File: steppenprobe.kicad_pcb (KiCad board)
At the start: 2 copper layers, 50 x 60 mm, 83 parts, among them J1 USB_C_Receptacle_USB2.0, J2 Conn_ST_STDC14, J4 Conn_01x16, Q1 2N7002, SW1 SW_SPDT, SW2 SW_Push, U1 FT2232H, U10 74LVC1G125, U11 74LVC1G125, U12 74LVC1G125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

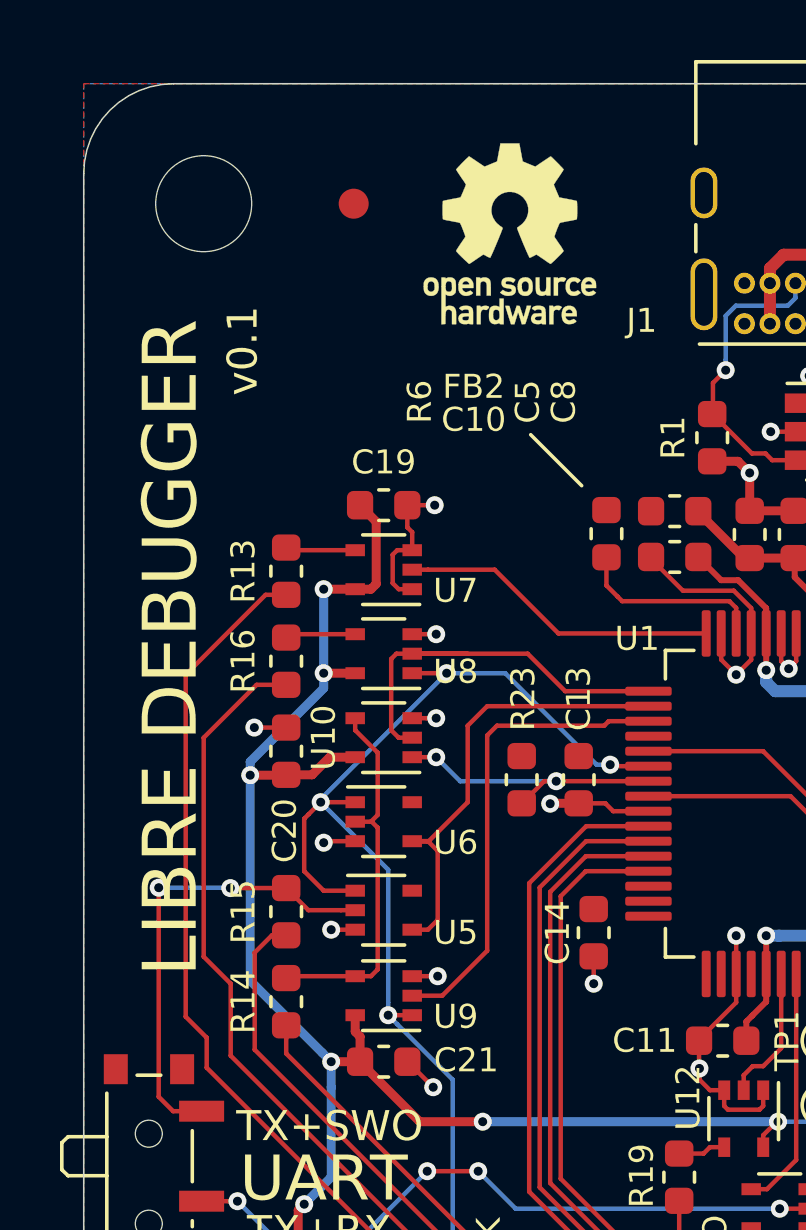
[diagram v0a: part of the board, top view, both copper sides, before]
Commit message: Add QR and new project URL. Finish bottom side silkscreen.
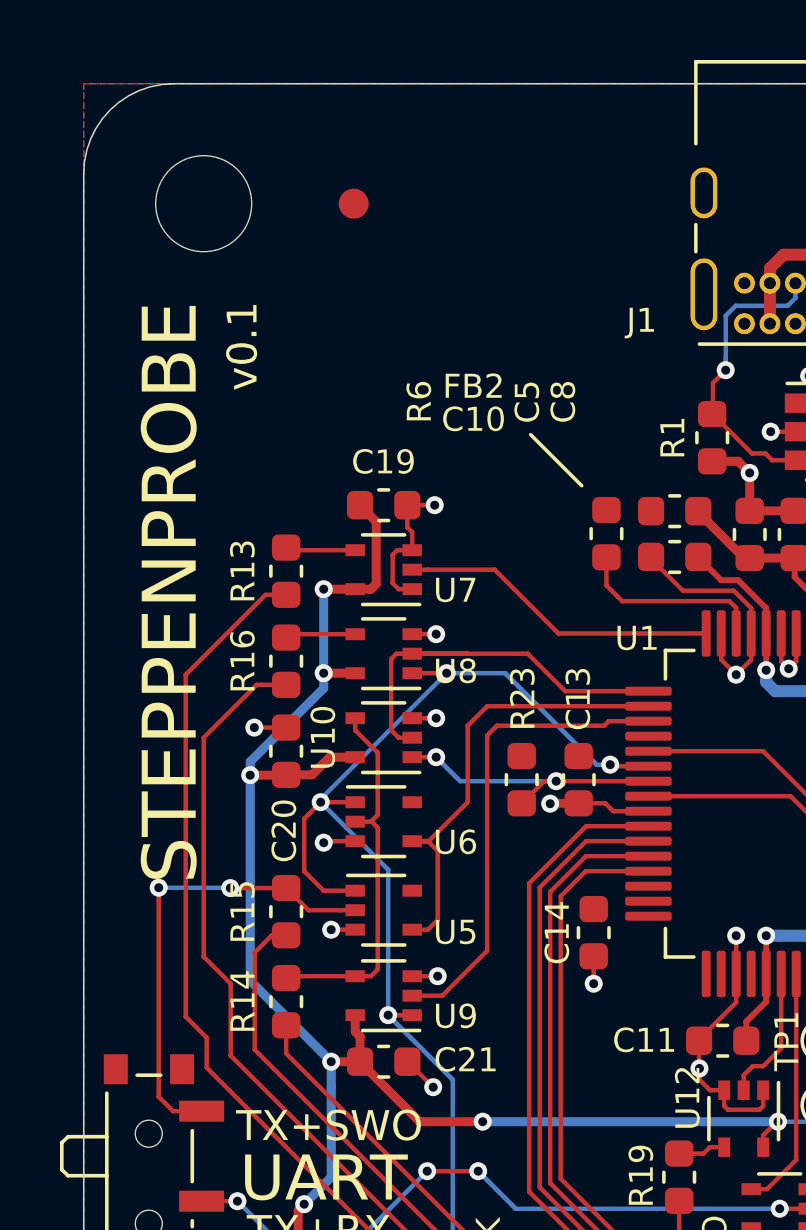
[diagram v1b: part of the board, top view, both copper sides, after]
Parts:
- added QR*****: qr_steppenprobe, Symbol:qr_steppenprobe, B.Cu at (125.0, 68.5)
- LOGO1: value Logo_Open_Hardware_Small -> Open Source Hardware; footprint Symbol:OSHW-Logo_5.7x6mm_SilkScreen -> Symbol:OSHW-Logo_7.5x8mm_SilkScreen; moved to B.Cu
- moved LOGO1 22.8 mm to (137.0, 55.0), turned to 180 degrees
- moved REF** 6.98 mm to (113.0, 55.0)
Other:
- board text added: "STEPPENPROBE"
- board text added: "github.com/diegoherranz/steppenprobe"
- board text removed: "LIBRE DEBUGGER"
- board text removed: "QR code!!!!!!!!"
- board text removed: "github.com/diegoherranz/libre-debugger"

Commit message: Replace reset switch and layout changes
- Reset switch SW_Push_1P1T_NO_E-Switch_TL3301NxxxxxG instead of SW_SPST_PTS645.
  The old one is smaller and not compatible (or at least too tight) with many easily sourceable 6mm switches.
  The new footprint should be compatible with many more options including the previous PTS645.
  Some small tweaks were required around it given its slightly bigger size.
- Version now v1.0
- GPIO names changed from 0-3 to A-D
- FTDI channel note made bigger and thicker. Now vertical left of the QR.
- QR not inverted anymore (some scanners struggled to read it).
- WEEE symbol added and symbols placed at the south end on the bottom side.
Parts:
- added R22: 10k, Resistor_SMD:R_0603_1608Metric, F.Cu at (112.9, 80.2)
- added R24: 10k, Resistor_SMD:R_0603_1608Metric, F.Cu at (133.8, 82.5)
- added REF**: WEEE-Logo_5.6x8mm_SilkScreen, Symbol:WEEE-Logo_5.6x8mm_SilkScreen, B.Cu at (112.5, 103.0)
- QR*****: value qr_steppenprobe -> qr_steppenprobe_neg; footprint Symbol:qr_steppenprobe -> Symbol:qr_steppenprobe_neg
- SW2: footprint Button_Switch_SMD:SW_SPST_PTS645 -> Button_Switch_SMD:SW_Push_1P1T_NO_E-Switch_TL3301NxxxxxG
- moved REF** 49.5 mm to (125.0, 103.0)
- moved LOGO1 48.0 mm to (137.5, 103.0)
- moved QR***** 3.50 mm to (125.0, 72.0)
- moved R8 0.34 mm to (143.3, 89.4), turned to 180 degrees
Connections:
- net /MPSSE_LED_K renamed /ACT_LED_K
- net /SWDIO_OE renamed /SWDIO_OE_N
- net /VDRIVE_R renamed /VDRIVE_TRGT
- J4 pad 12: /GPIO0 -> /GPIO_A
- J4 pad 13: /GPIO1 -> /GPIO_B
- J4 pad 14: /GPIO2 -> /GPIO_C
- J4 pad 15: /GPIO3 -> /GPIO_D
- Q1 pad 1: /SRST_N -> /SRST
- R7 pad 1: /MPSSE_LED_N -> /ACT_LED_N
- U1 pad 21: /SRST_N -> /ACT_LED_N
- U1 pad 24: /MPSSE_LED_N -> /SRST
- U1 pad 26: /GPIO0 -> Net-(U1-Pad26)
- U1 pad 27: /GPIO1 -> /GPIO_A
- U1 pad 28: /GPIO2 -> /GPIO_B
- U1 pad 29: /GPIO3 -> Net-(U1-Pad29)
- U1 pad 32: Net-(U1-Pad32) -> /GPIO_C
- U1 pad 33: Net-(U1-Pad33) -> /GPIO_D
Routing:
- net /GPIO3: track 42.2 -> 0.00 mm
- net /GPIO2: track 40.9 -> 0.00 mm
- net /GPIO1: track 39.3 -> 0.00 mm
- net /GPIO_B: track 0.00 -> 39.1 mm
- net /GPIO0: track 37.8 -> 0.00 mm
- net /GPIO_A: track 0.00 -> 37.6 mm
- net /GPIO_D: track 0.00 -> 36.0 mm
- net /GPIO_C: track 0.00 -> 36.0 mm
- net /ACT_LED_N: track 0.00 -> 27.0 mm
- net /MPSSE_LED_N: track 23.2 -> 0.00 mm
- net /SRST_N: track 20.7 -> 0.00 mm
- net /SRST: track 0.00 -> 20.0 mm
- net GND: track 104.9 -> 107.1 mm
- net /SWD_EN: track 52.8 -> 54.7 mm
- net /TMS: track 15.9 -> 16.8 mm
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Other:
- board text added: "(FROM TARGET)"
- board text added: "(MUST BE POWERED ON J2 OR J4)"
- board text added: "(TO TARGET)"
- board text added: "FTDI chip: CHANNEL A = JTAG/SWD+GPIOs CHANNEL B = UART"
- board text added: "GPIO_A"
- board text added: "GPIO_B"
- board text added: "GPIO_C"
- board text added: "GPIO_D"
- board text added: "RX"
- board text added: "v1.0"
- board text removed: "FTDI chip: CHANNEL A = JTAG/SWD + GPIOs CHANNEL B = UART"
- board text removed: "GPIO0"
- board text removed: "GPIO1"
- board text removed: "GPIO2"
- board text removed: "GPIO3"
- board text removed: "v0.1"

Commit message: Replace FT2232H by FT2232HL
Old symbol is no longer in the library. It was a common symbol for
both LQFP and QFN and it is now individual symbols for different
packages.
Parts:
- U1: value FT2232H -> FT2232HL

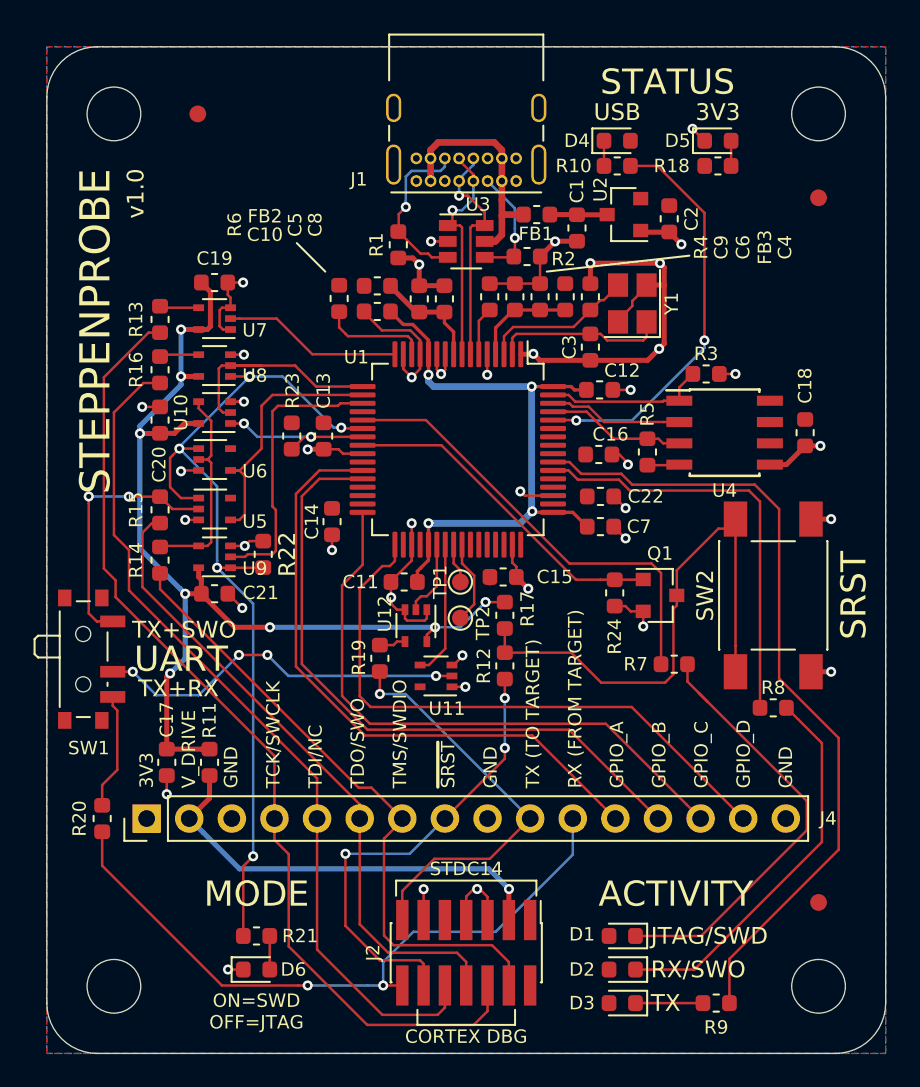
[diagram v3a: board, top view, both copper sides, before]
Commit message: Add pull up resistor to RXD_IN
To avoid spurious RX when floating.

Also some small tidy up of silkscreen designators.
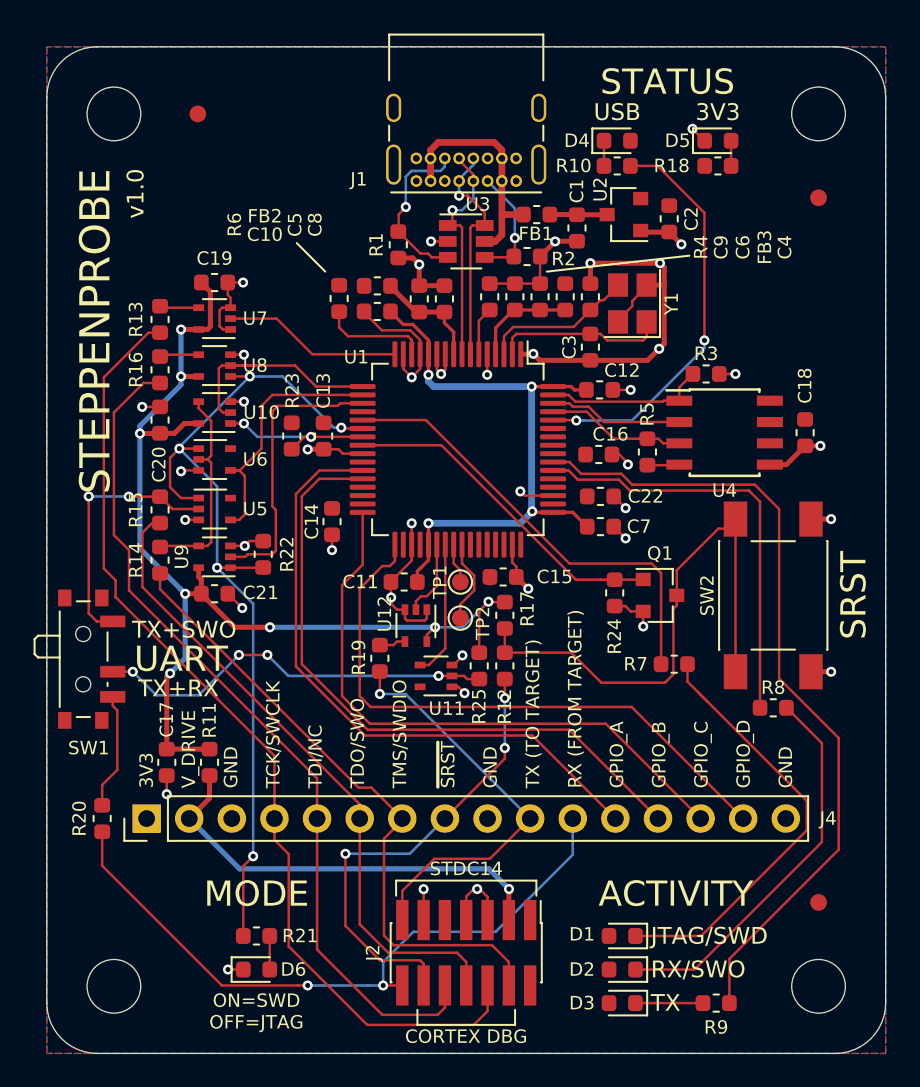
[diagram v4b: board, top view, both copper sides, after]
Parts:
- added R25: 100k, Resistor_SMD:R_0603_1608Metric, F.Cu at (125.8, 86.9)
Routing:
- net Vdrive: track 62.9 -> 66.3 mm
- net /RXD_IN: track 22.4 -> 24.1 mm

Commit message: LED resistors: 470R -> 1k     They were too bright. 1k may still be a bit too bright but if the current is reduced further, the LEDs which blink for brief instants, like the JTAG/SWD activity, get harder to see. Different resistors could be used for different LEDs, but for BOM simplicity, it was decided to stick with 1k everywhere.
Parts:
- R10, R18, R21, R7, R8, R9: value 470R -> 1k
